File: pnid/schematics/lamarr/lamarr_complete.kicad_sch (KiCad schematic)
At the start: 76 parts

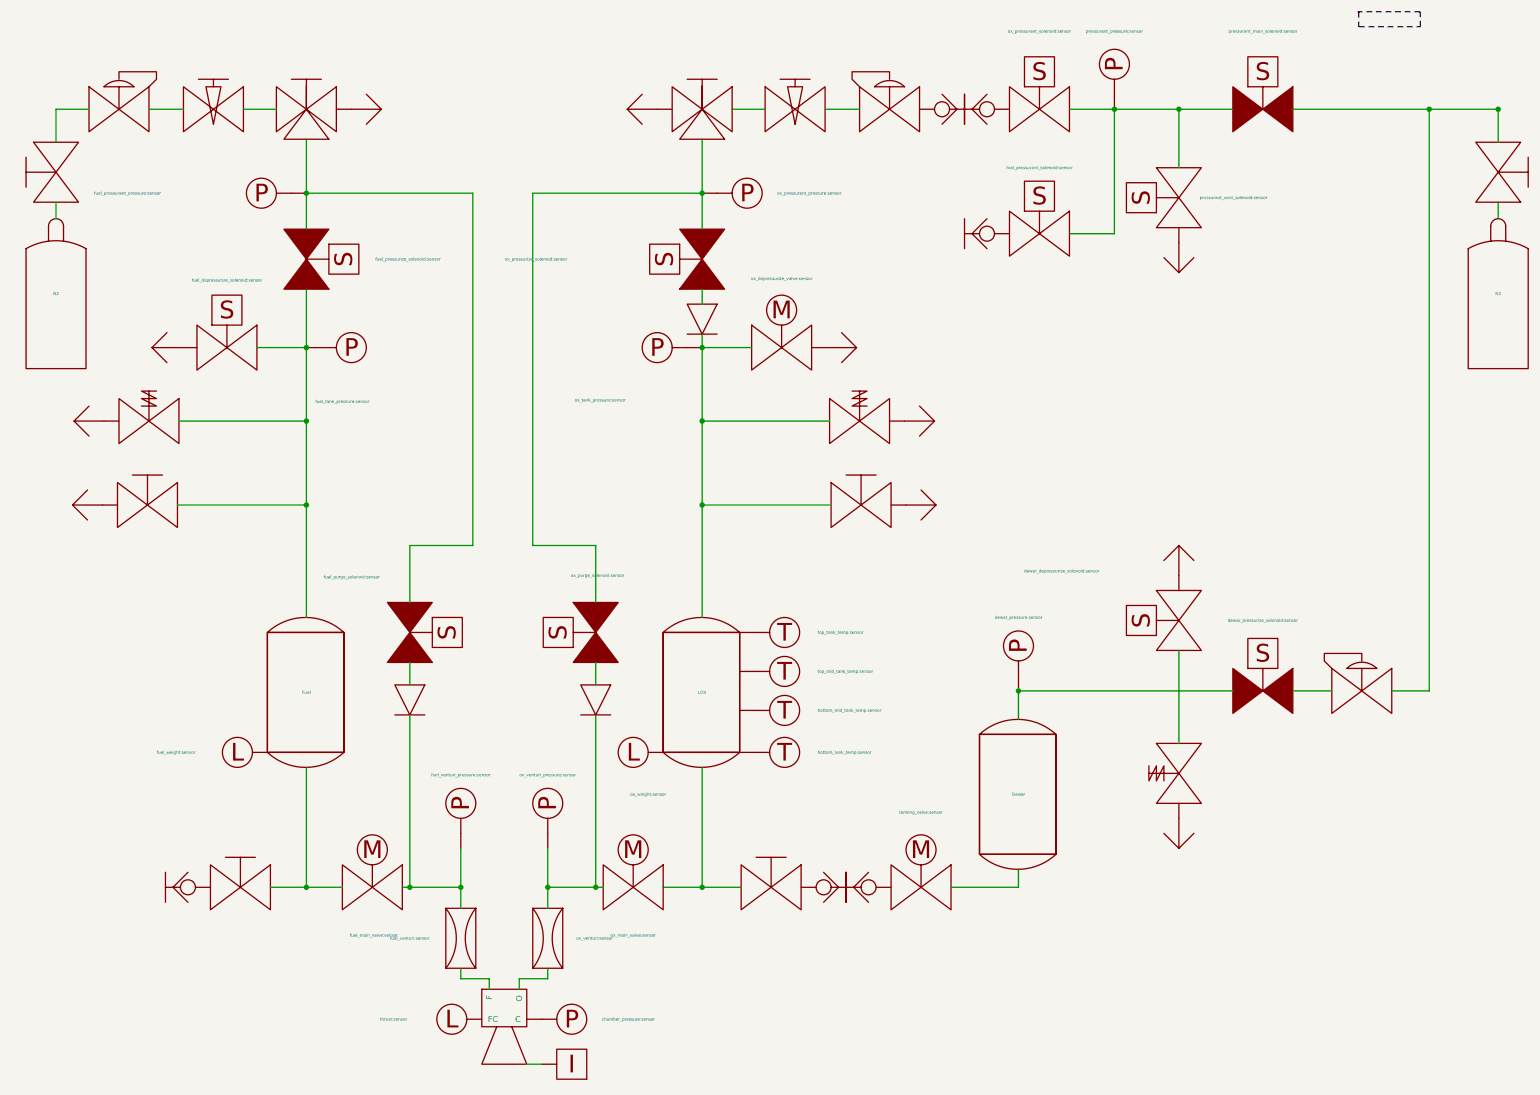
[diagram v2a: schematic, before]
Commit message: update label placement for lamarr_complete pnid
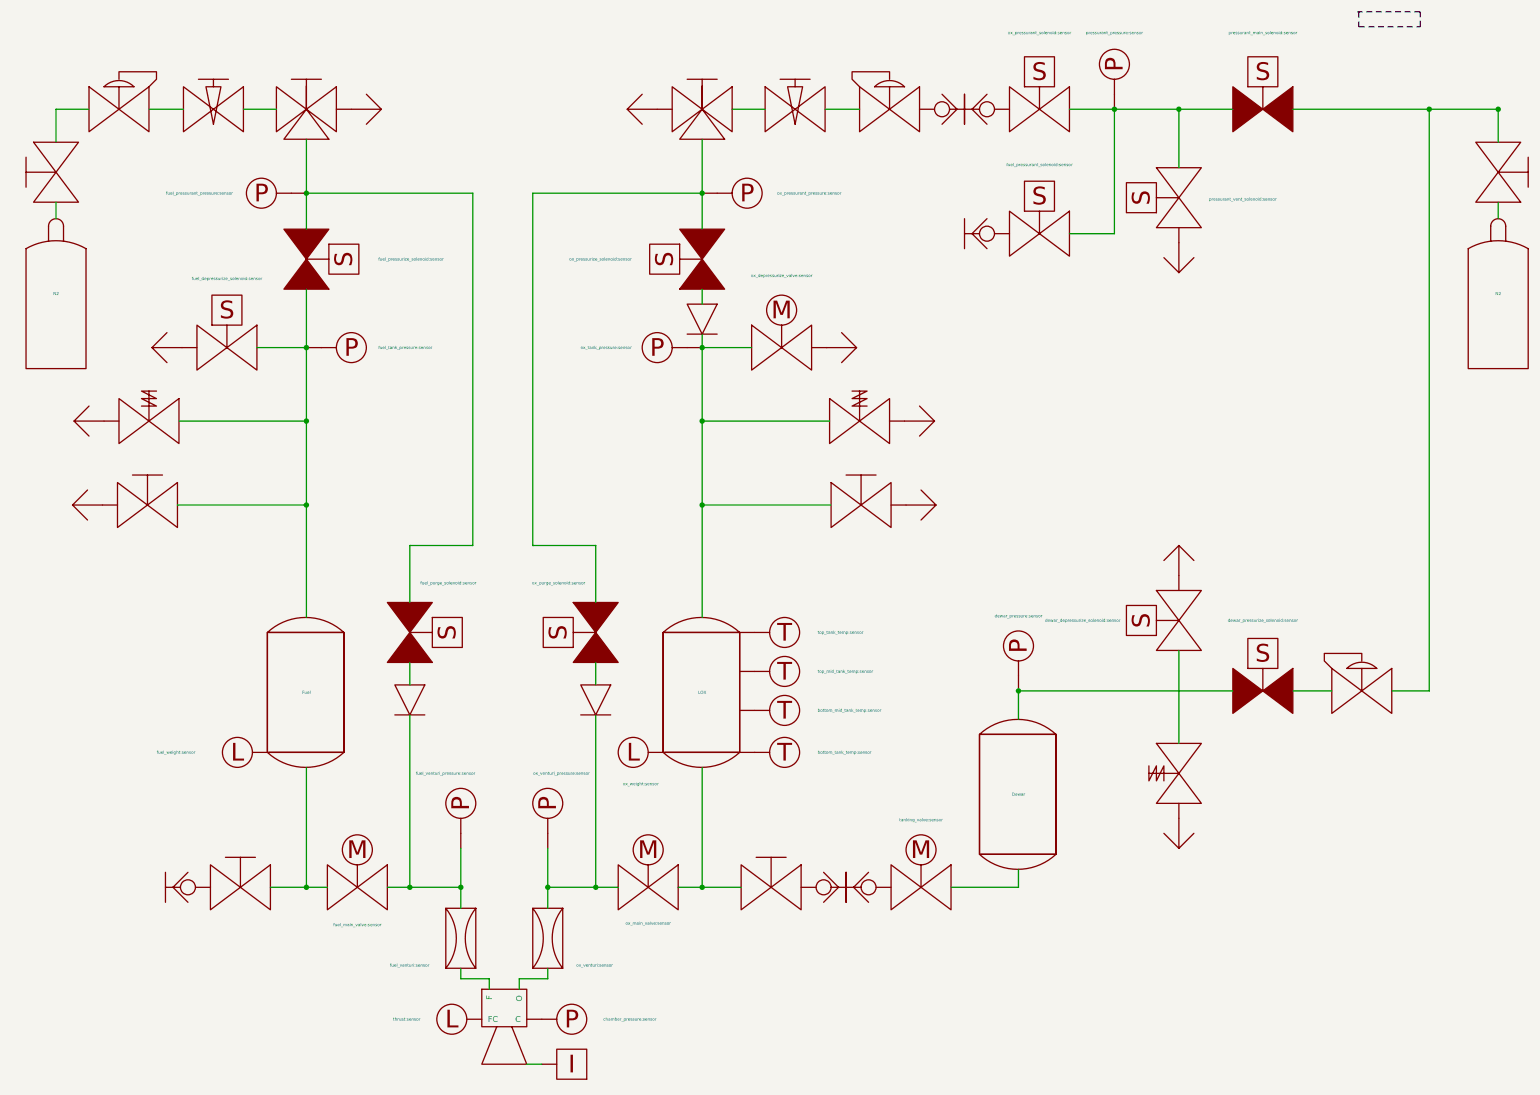
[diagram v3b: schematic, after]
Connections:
- net at engine.~ (O): now also thrust.~; no longer ox_venturi.~
- net at fuel_venturi.~: now also CheckValve?.~, fuel_main_valve.~, fuel_venturi_pressure.~; no longer engine.~ (O)
- net at DewarPressureRegulator?.~: now also ox_manual_valve.~, pressurant_main_solenoid?.~; no longer dewar_pressurize_solenoid?.~
- net at DewarOverPressureValve?.~: now also Vent?.~; no longer dewar_depressurize_solenoid?.~
- new net: fuel_manual_3way?., ox_pressurant_pressure:sensor.~, ox_pressurize_solenoid.~, ox_purge_solenoid.~
- new net: fuel_manual_3way., fuel_pressurant_pressure.~, fuel_pressurize_solenoid.~, fuel_purge_solenoid.~
- new net: Fuel.~, fuel_depressurize_solenoid.~, fuel_manual_vent_valve.~, fuel_pressurize_solenoid.~, fuel_safety_valve.~, fuel_tank_pressure.~
- new net: CheckValve?.~, LOX.~, ox_depressurize_valve.~, ox_manual_vent_valve.~, ox_safety_valve.~, ox_tank_pressure.~
- new net: LOX.~, ox_main_valve.~, ox_manual_tanking_valve.~
- new net: Fuel.~, fuel_main_valve.~, fuel_manual_tanking_valve.~
- new net: engine.~ (O), ox_venturi.~
- new net: engine.~ (O), fuel_venturi.~
- new net: DewarPressureRegulator?.~, dewar_pressurize_solenoid?.~
- new net: DewarOverPressureValve?.~, dewar_depressurize_solenoid?.~
- new net: fuel_pressurant_solenoid?.~, ox_pressurant_solenoid?.~, pressurant_main_solenoid?.~, pressurant_pressure?.~, pressurant_vent_solenoid?.~
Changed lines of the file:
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@@
 	(wire
 		(pts
-			(xy 128.778 162.814) (xy 135.382 162.814)
+			(xy 131.318 162.814) (xy 135.382 162.814)
 		)
 		(stroke
@@
 	(wire
 		(pts
-			(xy 117.348 162.814) (xy 118.618 162.814)
+			(xy 117.348 162.814) (xy 121.158 162.814)
 		)
 		(stroke
@@
 	(wire
 		(pts
-			(xy 84.582 162.814) (xy 85.852 162.814)
+			(xy 82.042 162.814) (xy 85.852 162.814)
 		)
 		(stroke
@@
 	(wire
 		(pts
-			(xy 68.326 162.814) (xy 74.422 162.814)
+			(xy 68.326 162.814) (xy 71.882 162.814)
 		)
 		(stroke
@@
 		)
 		(property "Value" "fuel_pressurant_pressure:sensor"
-			(at 43.688 45.212 0)
+			(at 55.88 45.212 0)
 			(effects
 				(font
@@
 		)
 		(property "Value" "ox_pressurize_solenoid:sensor"
-			(at 112.522 56.388 90)
+			(at 123.444 56.388 90)
 			(effects
 				(font
@@
 		)
 		(property "Value" "fuel_pressurize_solenoid:sensor"
-			(at 80.01 56.388 90)
+			(at 80.518 56.388 90)
 			(effects
 				(font
@@
 		)
 		(property "Value" "ox_purge_solenoid:sensor"
-			(at 122.174 109.982 90)
+			(at 115.57 111.252 90)
 			(effects
 				(font
@@
 		)
 		(property "Value" "fuel_purge_solenoid:sensor"
-			(at 80.772 110.236 90)
+			(at 87.63 111.252 90)
 			(effects
 				(font
 					(size 0.508 0.508)
 				)
-				(justify right)
+				(justify left)
 			)
 		)
@@
 		)
 		(property "Value" "fuel_venturi_pressure:sensor"
-			(at 94.488 143.764 90)
+			(at 86.868 143.51 90)
 			(effects
 				(font
 					(size 0.508 0.508)
 				)
+				(justify right)
 			)
 		)
@@
 		)
 		(property "Value" "ox_venturi_pressure:sensor"
-			(at 109.22 143.764 90)
+			(at 116.332 143.51 90)
 			(effects
 				(font
 					(size 0.508 0.508)
 				)
+				(justify left)
 			)
 		)
@@
 		)
 		(property "Value" "chamber_pressure:sensor"
-			(at 118.364 185.166 0)
+			(at 118.618 185.166 0)
 			(effects
 				(font
@@
 		)
 		(property "Value" "ox_venturi:sensor"
-			(at 114.046 171.45 90)
+			(at 114.046 176.022 90)
 			(effects
 				(font
@@
 	)
 	(symbol
+		(lib_name "PnID-Lib:Venturi")
 		(lib_id "PnID-Lib:Venturi")
 		(at 94.488 171.45 270)
@@
 		)
 		(property "Value" "fuel_venturi:sensor"
-			(at 89.154 171.45 90)
+			(at 89.154 176.022 90)
 			(effects
 				(font
@@
 		)
 		(property "Value" "fuel_depressurize_solenoid:sensor"
-			(at 54.864 59.944 0)
+			(at 54.864 59.69 0)
 			(effects
 				(font
@@
 	)
 	(symbol
+		(lib_name "PnID-Lib:Valve_Servo")
 		(lib_id "PnID-Lib:Valve_Servo")
-		(at 79.502 162.814 0)
+		(at 76.962 162.814 0)
 		(unit 1)
 		(exclude_from_sim no)
@@
 		(dnp no)
 		(property "Reference" "fuel_main_valve"
-			(at 79.502 151.5618 0)
+			(at 76.962 151.5618 0)
 			(effects
 				(font
@@
 		)
 		(property "Value" "fuel_main_valve:sensor"
-			(at 79.756 170.942 0)
+			(at 76.962 169.164 0)
 			(effects
 				(font
@@
 		)
 		(property "Footprint" ""
-			(at 79.502 162.814 0)
+			(at 76.962 162.814 0)
 			(effects
 				(font
@@
 		)
 		(property "Datasheet" ""
-			(at 79.502 162.814 0)
+			(at 76.962 162.814 0)
 			(effects
 				(font
@@
 		)
 		(property "Description" ""
-			(at 79.502 162.814 0)
+			(at 76.962 162.814 0)
 			(effects
 				(font
@@
 		)
 		(property "Unit" "%"
-			(at 79.502 162.814 0)
+			(at 76.962 162.814 0)
 			(effects
 				(font
@@
 		)
 		(property "Action_Reference" " "
-			(at 79.502 162.814 0)
+			(at 76.962 162.814 0)
 			(effects
 				(font
@@
 	)
 	(symbol
+		(lib_name "PnID-Lib:Valve_Solenoid_NC")
 		(lib_id "PnID-Lib:Valve_Solenoid_NC")
 		(at 230.378 129.54 0)
@@
 		)
 		(property "Value" "dewar_pressure:sensor"
-			(at 188.976 117.094 90)
+			(at 188.976 116.84 90)
 			(effects
 				(font
@@
 		)
 		(property "Value" "tanking_valve:sensor"
-			(at 172.466 150.114 0)
+			(at 172.466 151.384 0)
 			(effects
 				(font
@@
 		)
 		(property "Value" "pressurant_main_solenoid:sensor"
-			(at 230.378 17.78 0)
+			(at 230.378 18.034 0)
 			(effects
 				(font
@@
 		)
 		(property "Value" "pressurant_vent_solenoid:sensor"
-			(at 231.14 45.974 90)
+			(at 221.234 46.228 90)
 			(effects
 				(font
 					(size 0.508 0.508)
 				)
-				(justify left)
+				(justify right)
 			)
 		)
@@
 		)
 		(property "Value" "pressurant_pressure:sensor"
-			(at 205.232 17.78 90)
+			(at 205.232 18.034 90)
 			(effects
 				(font
@@
 		)
 		(property "Value" "fuel_pressurant_solenoid:sensor"
-			(at 192.532 40.894 0)
+			(at 192.532 40.386 0)
 			(effects
 				(font
@@
 		)
 		(property "Value" "ox_pressurant_solenoid:sensor"
-			(at 192.532 17.78 0)
+			(at 192.532 18.034 0)
 			(effects
 				(font
@@
 	)
 	(symbol
+		(lib_name "PnID-Lib:Valve_Solenoid_NO")
 		(lib_id "PnID-Lib:Valve_Solenoid_NO")
 		(at 216.154 117.602 90)
@@
 		)
 		(property "Value" "dewar_depressurize_solenoid:sensor"
-			(at 202.692 109.22 90)
+			(at 206.248 117.602 90)
 			(effects
 				(font
@@
 		)
 		(property "Value" "ox_depressurize_valve:sensor"
-			(at 148.844 59.69 0)
+			(at 148.844 59.182 0)
 			(effects
 				(font
@@
 		)
 		(property "Value" "fuel_tank_pressure:sensor"
-			(at 69.85 80.518 0)
+			(at 80.518 71.374 0)
 			(effects
 				(font
@@
 		)
 		(property "Value" "ox_tank_pressure:sensor"
-			(at 122.428 80.264 0)
+			(at 123.444 71.374 0)
 			(effects
 				(font
@@
 		(lib_name "PnID-Lib:Valve_Servo")
 		(lib_id "PnID-Lib:Valve_Servo")
-		(at 123.698 162.814 0)
+		(at 126.238 162.814 0)
 		(unit 1)
 		(exclude_from_sim no)
@@
 		(dnp no)
 		(property "Reference" "ox_main_valve"
-			(at 123.698 151.5618 0)
+			(at 126.238 151.5618 0)
 			(effects
 				(font
@@
 		)
 		(property "Value" "ox_main_valve:sensor"
-			(at 123.698 170.942 0)
+			(at 126.238 168.91 0)
 			(effects
 				(font
@@
 		)
 		(property "Footprint" ""
-			(at 123.698 162.814 0)
+			(at 126.238 162.814 0)
 			(effects
 				(font
@@
 		)
 		(property "Datasheet" ""
-			(at 123.698 162.814 0)
+			(at 126.238 162.814 0)
 			(effects
 				(font
@@
 		)
 		(property "Description" ""
-			(at 123.698 162.814 0)
+			(at 126.238 162.814 0)
 			(effects
 				(font
@@
 		)
 		(property "Unit" "%"
-			(at 123.698 162.814 0)
+			(at 126.238 162.814 0)
 			(effects
 				(font
@@
 		)
 		(property "Action_Reference" " "
-			(at 123.698 162.814 0)
+			(at 126.238 162.814 0)
 			(effects
 				(font
@@
 		)
 		(property "Value" "thrust:sensor"
-			(at 80.772 185.166 0)
+			(at 87.63 185.166 0)
 			(effects
 				(font
 					(size 0.508 0.508)
 				)
-				(justify right)
+				(justify left)
 			)
 		)
@@
 		)
 		(property "Value" "ox_weight:sensor"
-			(at 126.238 147.066 0)
+			(at 124.968 145.288 0)
 			(effects
 				(font

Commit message: dump changes from hotfire prep
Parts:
- added U1: sound_supression:sensor, symbol PnID-Lib:Pump
- added heater1: tank_heating:sensor, symbol PnID-Lib:heater
- added ox_purge_solenoid1: safety_valves:sensor, symbol PnID-Lib:Valve_Solenoid_NC
- ox_depressurize_valve: symbol PnID-Lib:Valve_Servo -> PnID-Lib:Valve_Solenoid_NO
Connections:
- net at engine.~ (O): now also thrust.~; no longer ox_venturi.~
- net at fuel_venturi.~: now also CheckValve?.~, fuel_main_valve.~, fuel_venturi_pressure.~; no longer engine.~ (O)
- net at DewarPressureRegulator?.~: now also ox_manual_valve.~, pressurant_main_solenoid?.~; no longer dewar_pressurize_solenoid?.~
- net at DewarOverPressureValve?.~: now also Vent?.~; no longer dewar_depressurize_solenoid?.~
- new net: fuel_manual_3way?., ox_pressurant_pressure:sensor.~, ox_pressurize_solenoid.~, ox_purge_solenoid.~
- new net: fuel_manual_3way., fuel_pressurant_pressure.~, fuel_pressurize_solenoid.~, fuel_purge_solenoid.~
- new net: Fuel.~, fuel_depressurize_solenoid.~, fuel_manual_vent_valve.~, fuel_pressurize_solenoid.~, fuel_safety_valve.~, fuel_tank_pressure.~
- new net: CheckValve?.~, LOX.~, ox_depressurize_valve.~, ox_manual_vent_valve.~, ox_safety_valve.~, ox_tank_pressure.~
- new net: LOX.~, ox_main_valve.~, ox_manual_tanking_valve.~
- new net: Fuel.~, fuel_main_valve.~, fuel_manual_tanking_valve.~
- new net: engine.~ (O), ox_venturi.~
- new net: engine.~ (O), fuel_venturi.~
- new net: DewarPressureRegulator?.~, dewar_pressurize_solenoid?.~
- new net: DewarOverPressureValve?.~, dewar_depressurize_solenoid?.~
- new net: fuel_pressurant_solenoid?.~, ox_pressurant_solenoid?.~, pressurant_main_solenoid?.~, pressurant_pressure?.~, pressurant_vent_solenoid?.~
